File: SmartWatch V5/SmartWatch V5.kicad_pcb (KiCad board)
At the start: 4 copper layers, 23.7 x 34.2 mm, 61 parts, among them J1 10118192-0001LF, J10 TestPad, J2 , J8 TestPad, J9 TestPad, Q1 FDN340P, Q2 MMBT3904, Q3 MMBT3904, Q4 FDN028N20, Q5 FDN028N20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

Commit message: Changed ACCEL_EN to IO34
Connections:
- U6 pad 28: /ACCEL_EN -> (no net)
- U6 pad 6: (no net) -> /ACCEL_EN
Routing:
- net /ACCEL_EN: track 29.6 -> 26.6 mm
- net /EN: track 44.4 -> 43.0 mm
- net /LCD_EN: track 22.7 -> 21.9 mm

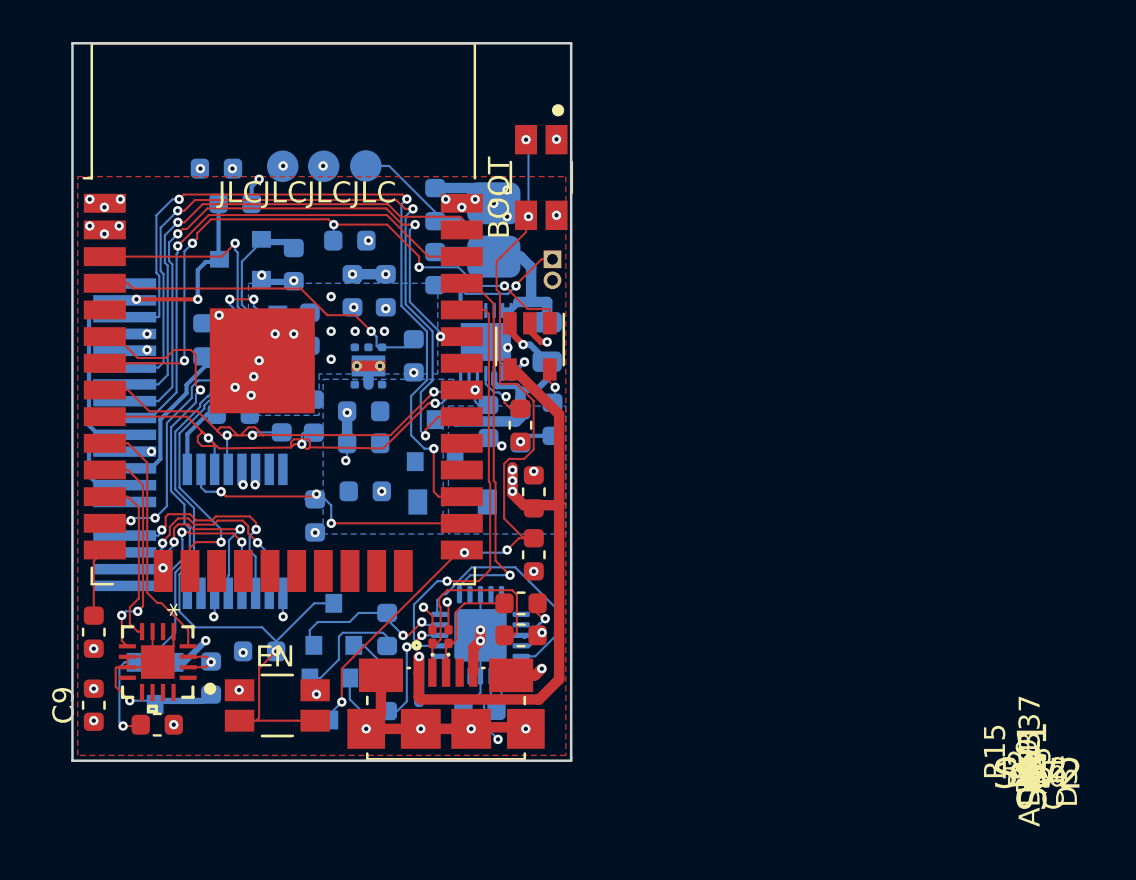
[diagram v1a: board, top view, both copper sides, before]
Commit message: Rerouted ACCEL_EN to IO34
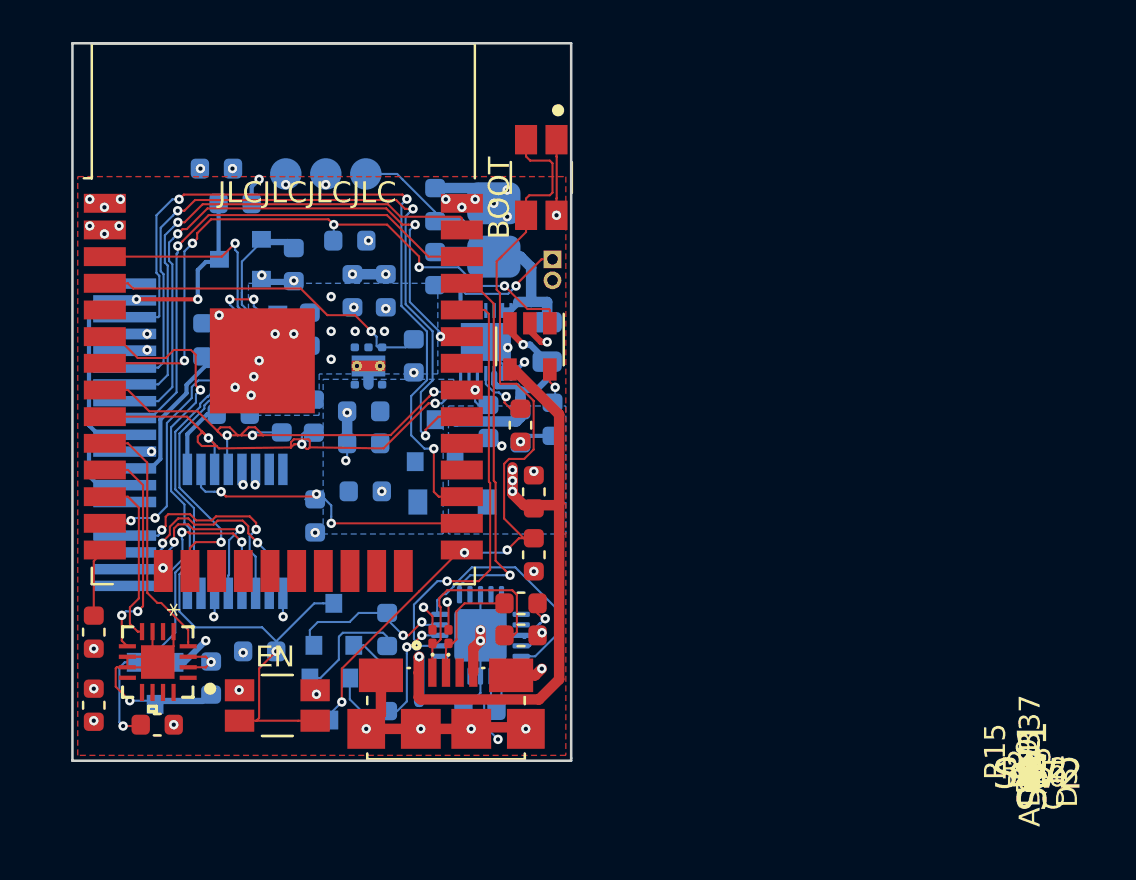
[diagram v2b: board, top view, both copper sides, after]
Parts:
- moved J10 0.39 mm to (91.1, 71.9)
- moved J8 0.38 mm to (94.9, 71.9)
- moved J9 0.38 mm to (93.0, 71.9)
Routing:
- net GND: track 54.5 -> 58.1 mm, vias 52 -> 51
- net /IO0: track 37.5 -> 39.4 mm, vias 5 -> 3
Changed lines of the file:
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@@
     (thickness 1.6)
     (drawings 17)
-    (tracks 941)
+    (tracks 949)
     (zones 0)
     (modules 61)
@@
   (page A4)
   (layers
-    (0 F.Cu signal)
-    (1 In1.Cu signal)
-    (2 In2.Cu signal)
-    (31 B.Cu signal)
+    (0 F.Cu signal hide)
+    (1 In1.Cu signal hide)
+    (2 In2.Cu signal hide)
+    (31 B.Cu signal hide)
     (32 B.Adhes user hide)
     (33 F.Adhes user hide)
@@
     (35 F.Paste user hide)
     (36 B.SilkS user)
-    (37 F.SilkS user)
+    (37 F.SilkS user hide)
     (38 B.Mask user hide)
     (39 F.Mask user hide)
     (40 Dwgs.User user hide)
-    (41 Cmts.User user)
-    (42 Eco1.User user)
-    (43 Eco2.User user)
-    (44 Edge.Cuts user)
-    (45 Margin user)
-    (46 B.CrtYd user)
-    (47 F.CrtYd user)
-    (48 B.Fab user)
+    (41 Cmts.User user hide)
+    (42 Eco1.User user hide)
+    (43 Eco2.User user hide)
+    (44 Edge.Cuts user hide)
+    (45 Margin user hide)
+    (46 B.CrtYd user hide)
+    (47 F.CrtYd user hide)
+    (48 B.Fab user hide)
     (49 F.Fab user hide)
   )
@@
     (tags capacitor)
     (attr smd)
-    (fp_text reference C15 (at 0 1.43 90) (layer B.SilkS)
+    (fp_text reference C15 (at -18.6435 45.466 90) (layer B.SilkS)
       (effects (font (size 1 1) (thickness 0.15)) (justify mirror))
     )
@@
     (tags capacitor)
     (attr smd)
-    (fp_text reference C14 (at 0 1.43) (layer B.SilkS)
+    (fp_text reference C14 (at 44.831 25.4) (layer B.SilkS)
       (effects (font (size 1 1) (thickness 0.15)) (justify mirror))
     )
@@
     (tags capacitor)
     (attr smd)
-    (fp_text reference C13 (at 0 1.43 270) (layer B.SilkS)
+    (fp_text reference C13 (at 2.159 -45.212 270) (layer B.SilkS)
       (effects (font (size 1 1) (thickness 0.15)) (justify mirror))
     )
@@
     (tags capacitor)
     (attr smd)
-    (fp_text reference C9 (at 0 -1.43 90) (layer F.SilkS)
+    (fp_text reference C9 (at -3.2765 44.577 90) (layer F.SilkS)
       (effects (font (size 1 1) (thickness 0.15)))
     )
@@
     (tags capacitor)
     (attr smd)
-    (fp_text reference C6 (at 0 1.43) (layer B.SilkS)
+    (fp_text reference C6 (at 37.6175 11.049) (layer B.SilkS)
       (effects (font (size 1 1) (thickness 0.15)) (justify mirror))
     )
@@
   )
   (module CustomFootprints:TESTPAD (layer B.Cu)
-    (at 90.914 71.517)
+    (at 91.059 71.882)
     (fp_text reference J10 (at 41.42 26.273) (layer B.SilkS)
       (effects (font (size 1 1) (thickness 0.15)) (justify mirror))
@@
   )
   (module CustomFootprints:TESTPAD (layer B.Cu)
-    (at 92.864 71.517)
+    (at 92.964 71.882)
     (fp_text reference J9 (at 39.216 27.035) (layer B.SilkS)
       (effects (font (size 1 1) (thickness 0.15)) (justify mirror))
@@
   )
   (module CustomFootprints:TESTPAD (layer B.Cu)
-    (at 94.869 71.501)
+    (at 94.869 71.882)
     (fp_text reference J8 (at 37.719 27.305) (layer B.SilkS)
       (effects (font (size 1 1) (thickness 0.15)) (justify mirror))
@@
     (arrow2b (pts (xy 65.600001 65.6) (xy 66.186422 66.726504)))
   )
+  (via (at 91.059 72.39) (size 0.45) (drill 0.2) (layers F.Cu B.Cu) (net 13))
+  (via (at 92.964 72.39) (size 0.45) (drill 0.2) (layers F.Cu B.Cu) (net 7))
   (segment (start 88.971 89.4155) (end 88.9635 89.408) (width 0.1) (layer B.Cu) (net 1))
   (via (at 88.9635 89.408) (size 0.45) (drill 0.2) (layers F.Cu B.Cu) (net 1))
@@
   (via (at 84.661991 85.097798) (size 0.45) (drill 0.2) (layers F.Cu B.Cu) (net 7))
   (segment (start 84.343793 85.097798) (end 84.661991 85.097798) (width 0.2) (layer B.Cu) (net 7))
-  (via (at 92.837 71.501) (size 0.45) (drill 0.2) (layers F.Cu B.Cu) (net 7))
   (segment (start 92.864 71.517) (end 92.853 71.517) (width 0.1) (layer B.Cu) (net 7))
   (segment (start 92.853 71.517) (end 92.837 71.501) (width 0.1) (layer B.Cu) (net 7))
@@
   (via (at 87.884 78.613) (size 0.45) (drill 0.2) (layers F.Cu B.Cu) (net 13))
   (via (at 90.551 79.502) (size 0.45) (drill 0.2) (layers F.Cu B.Cu) (net 13))
-  (via (at 103.9495 70.231) (size 0.45) (drill 0.2) (layers F.Cu B.Cu) (net 13))
   (via (at 103.9495 73.8505) (size 0.45) (drill 0.2) (layers F.Cu B.Cu) (net 13))
   (via (at 101.6 73.914) (size 0.45) (drill 0.2) (layers F.Cu B.Cu) (net 13))
@@
   (segment (start 98.044 92.941964) (end 97.616445 92.514409) (width 0.1) (layer F.Cu) (net 13))
   (segment (start 98.044 93.594) (end 98.044 92.941964) (width 0.1) (layer F.Cu) (net 13))
-  (via (at 90.932 71.501) (size 0.45) (drill 0.2) (layers F.Cu B.Cu) (net 13))
   (segment (start 90.914 71.517) (end 90.916 71.517) (width 0.1) (layer B.Cu) (net 13))
   (segment (start 90.916 71.517) (end 90.932 71.501) (width 0.1) (layer B.Cu) (net 13))
@@
   (via (at 89.789 80.772) (size 0.45) (drill 0.2) (layers F.Cu B.Cu) (net 13))
   (via (at 88.646 82.042) (size 0.45) (drill 0.2) (layers F.Cu B.Cu) (net 13))
+  (segment (start 103.95901 71.06001) (end 103.95901 73.04099) (width 0.1) (layer F.Cu) (net 13))
+  (segment (start 103.9495 71.0505) (end 103.95901 71.06001) (width 0.1) (layer F.Cu) (net 13))
+  (segment (start 103.95901 73.04099) (end 103.9495 73.0505) (width 0.1) (layer F.Cu) (net 13))
+  (segment (start 103.9495 73.0505) (end 103.9495 73.8505) (width 0.1) (layer F.Cu) (net 13))
+  (segment (start 103.9495 70.2505) (end 103.9495 71.0505) (width 0.1) (layer F.Cu) (net 13))
   (segment (start 103.505 77.978) (end 103.505 78.9455) (width 0.5) (layer B.Cu) (net 14))
   (segment (start 102.124 78.020601) (end 102.124 77.978) (width 0.3) (layer B.Cu) (net 14))
@@
   (segment (start 102.743 77.978) (end 103.505 77.978) (width 0.5) (layer B.Cu) (net 14))
   (segment (start 98.171 73.6925) (end 98.171 74.13) (width 0.1) (layer B.Cu) (net 14))
-  (segment (start 95.9795 71.501) (end 98.171 73.6925) (width 0.1) (layer B.Cu) (net 14))
-  (segment (start 94.869 71.501) (end 95.9795 71.501) (width 0.1) (layer B.Cu) (net 14))
+  (segment (start 96.3605 71.882) (end 94.869 71.882) (width 0.1) (layer B.Cu) (net 14))
+  (segment (start 96.63075 72.15225) (end 96.3605 71.882) (width 0.1) (layer B.Cu) (net 14))
+  (segment (start 96.63075 72.15225) (end 98.171 73.6925) (width 0.1) (layer B.Cu) (net 14))
   (segment (start 101.33 97.171) (end 101.092 97.409) (width 0.1) (layer B.Cu) (net 16))
   (segment (start 101.33 95.7905) (end 101.33 97.171) (width 0.1) (layer B.Cu) (net 16))
@@
   (segment (start 93.157 97.597) (end 93.157 97.885) (width 0.1) (layer B.Cu) (net 23))
   (segment (start 93.726 97.028) (end 93.157 97.597) (width 0.1) (layer B.Cu) (net 23))
-  (via (at 102.616 73.914) (size 0.45) (drill 0.2) (layers F.Cu B.Cu) (net 23))
-  (segment (start 102.4995 73.8505) (end 102.5525 73.8505) (width 0.1) (layer F.Cu) (net 23))
-  (segment (start 102.5525 73.8505) (end 102.616 73.914) (width 0.1) (layer F.Cu) (net 23))
-  (via (at 102.4995 70.2505) (size 0.45) (drill 0.2) (layers F.Cu B.Cu) (net 23))
-  (segment (start 102.616 73.914) (end 102.616 70.367) (width 0.1) (layer B.Cu) (net 23))
-  (segment (start 102.616 70.367) (end 102.4995 70.2505) (width 0.1) (layer B.Cu) (net 23))
   (segment (start 102.86001 85.004498) (end 102.412518 85.45199) (width 0.1) (layer F.Cu) (net 23))
   (segment (start 101.097998 76.052002) (end 101.097998 77.396002) (width 0.1) (layer F.Cu) (net 23))
@@
   (segment (start 101.275 75.875) (end 101.097998 76.052002) (width 0.1) (layer F.Cu) (net 23))
   (segment (start 102.047509 81.874001) (end 102.86001 82.686502) (width 0.1) (layer F.Cu) (net 23))
+  (segment (start 102.4995 71.0505) (end 102.4995 70.2505) (width 0.1) (layer F.Cu) (net 23))
+  (segment (start 102.4995 71.0505) (end 102.696 71.247) (width 0.1) (layer F.Cu) (net 23))
+  (segment (start 102.696 71.247) (end 103.632 71.247) (width 0.1) (layer F.Cu) (net 23))
+  (segment (start 103.632 71.247) (end 103.759 71.374) (width 0.1) (layer F.Cu) (net 23))
+  (segment (start 102.4995 73.0505) (end 102.4995 73.8505) (width 0.1) (layer F.Cu) (net 23))
+  (segment (start 102.652 72.898) (end 102.4995 73.0505) (width 0.1) (layer F.Cu) (net 23))
+  (segment (start 103.632 72.898) (end 103.759 72.771) (width 0.1) (layer F.Cu) (net 23))
+  (segment (start 103.759 71.374) (end 103.759 72.771) (width 0.1) (layer F.Cu) (net 23))
+  (segment (start 103.632 72.898) (end 102.652 72.898) (width 0.1) (layer F.Cu) (net 23))
   (via (at 97.536 93.853) (size 0.45) (drill 0.2) (layers F.Cu B.Cu) (net 24))
   (segment (start 98.3925 93.853) (end 97.536 93.853) (width 0.1) (layer B.Cu) (net 24))
@@
     )
   )
-  (zone (net 13) (net_name GND) (layer In2.Cu) (hatch edge 0.508)
-    (connect_pads (clearance 0.15))
-    (min_thickness 0.254)
-    (fill yes (arc_segments 32) (thermal_gap 0.45) (thermal_bridge_width 0.508))
-    (polygon
-      (pts
-        (xy 104.394 99.568) (xy 81.153 99.568) (xy 81.153 71.501) (xy 104.394 71.501)
-      )
-    )
-  )
   (zone (net 7) (net_name +3V3) (layer B.Cu) (hatch edge 0.508)
     (connect_pads (clearance 0.15))
@@
       )
     )
+  )
+  (zone (net 13) (net_name GND) (layer In2.Cu) (hatch edge 0.508)
+    (connect_pads (clearance 0.15))
+    (min_thickness 0.254)
+    (fill yes (arc_segments 32) (thermal_gap 0.45) (thermal_bridge_width 0.508))
+    (polygon
+      (pts
+        (xy 104.394 99.568) (xy 81.153 99.568) (xy 81.153 71.501) (xy 104.394 71.501)
+      )
+    )
